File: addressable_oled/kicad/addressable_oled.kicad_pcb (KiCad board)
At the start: 2 copper layers, 1 part

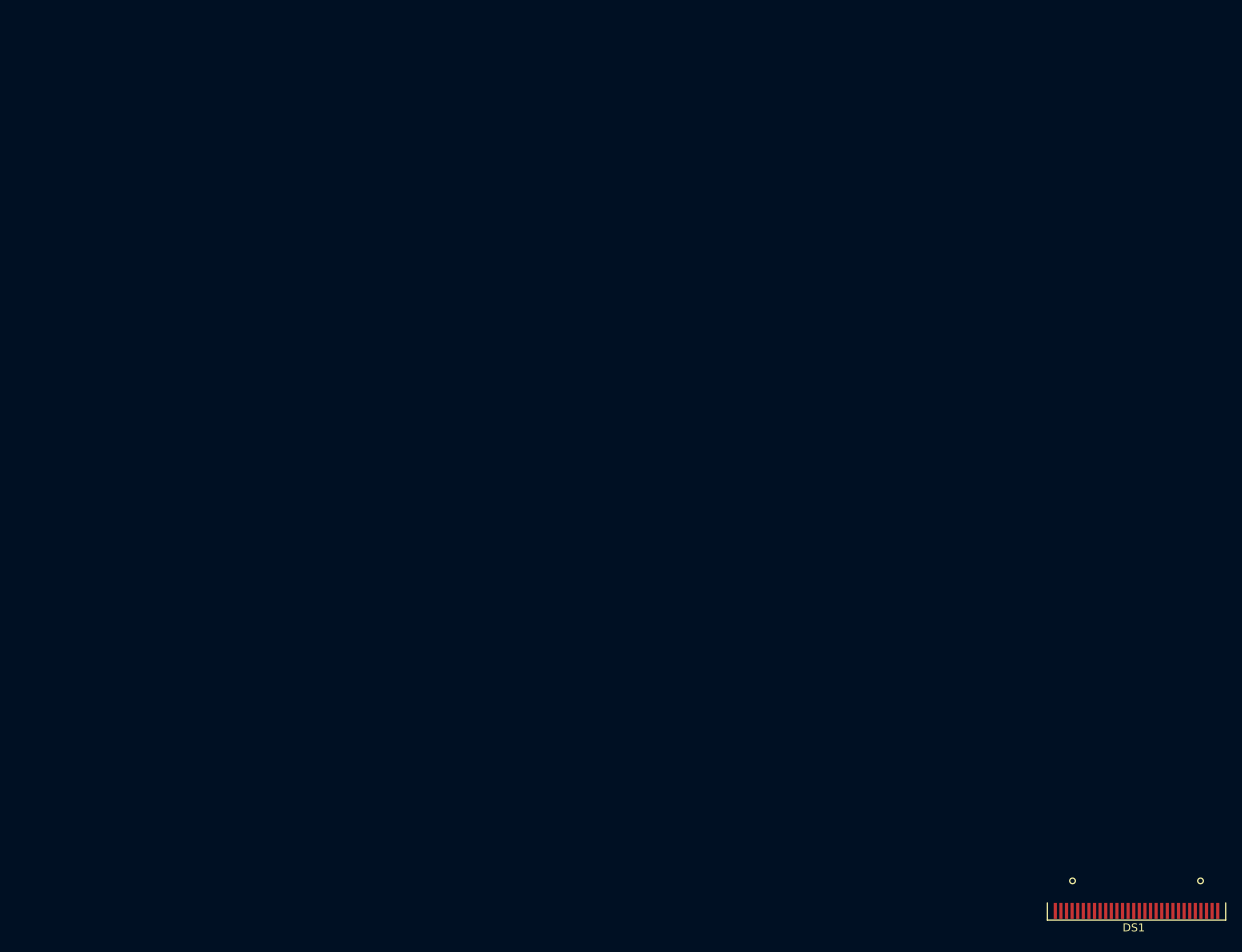
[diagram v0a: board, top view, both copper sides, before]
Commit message: Work in progress. Added symbols and footprints.
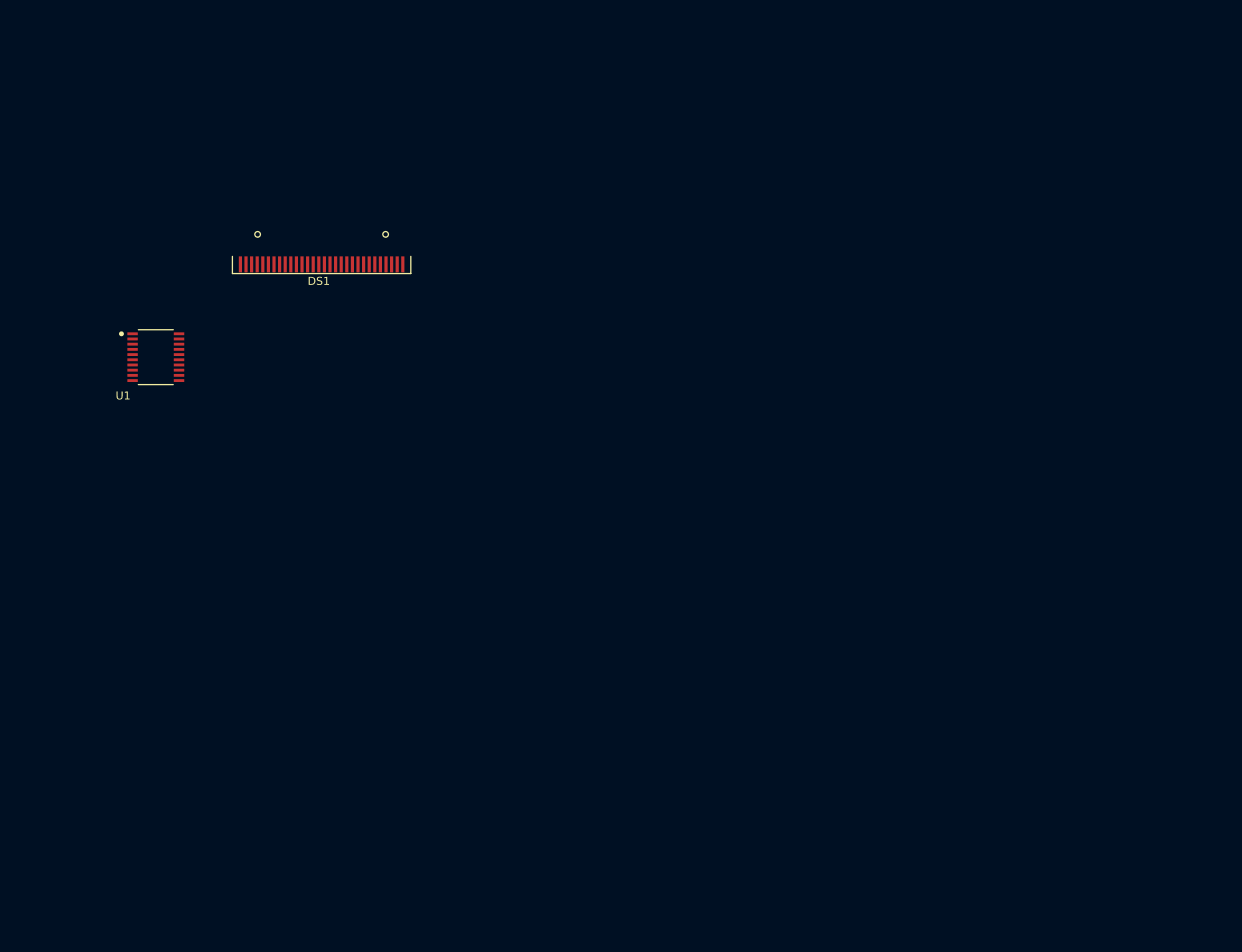
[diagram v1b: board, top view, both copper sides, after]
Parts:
- added U1: SLG46826G, addressable_oled:TSSOP20_MO-220_WECE_REN, F.Cu at (-1.32, 24.2)
- DS1: footprint Display:OLED-128O064D -> addressable_oled:OLED-128O064D
- moved DS1 130.0 mm to (19.4, 12.6)

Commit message: More progress with the schematic and layout.
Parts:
- added C1: 100n, Capacitor_SMD:C_0603_1608Metric, F.Cu at (-7.29, -11.4)
- added C2: 100n, Capacitor_SMD:C_0603_1608Metric, F.Cu at (-7.29, -8.90)
- added C3: 2u2, Capacitor_SMD:C_0603_1608Metric, F.Cu at (-7.29, -6.39)
- added C4: 1u, Capacitor_SMD:C_0603_1608Metric, F.Cu at (-7.29, -3.88)
- added C5: 1u, Capacitor_SMD:C_0603_1608Metric, F.Cu at (-3.28, -11.4)
- added C6: 100n, Capacitor_SMD:C_0603_1608Metric, F.Cu at (-3.28, -8.90)
- added C7: 100n, Capacitor_SMD:C_0603_1608Metric, F.Cu at (-3.28, -6.39)
- added C8: 100n, Capacitor_SMD:C_0603_1608Metric, F.Cu at (-3.28, -3.88)
- added C9: 2u2, Capacitor_SMD:C_0603_1608Metric, F.Cu at (0.73, -11.4)
- added J1: Conn_01x05_Pin, Connector_PinHeader_2.54mm:PinHeader_1x05_P2.54mm_Vertical, F.Cu at (15.1, -13.2)
- added J2: Conn_01x03_Socket, Connector_PinHeader_2.54mm:PinHeader_1x03_P2.54mm_Vertical, F.Cu at (42.4, 4.19)
- added JP1: Jumper_2_Open, Jumper:SolderJumper-2_P1.3mm_Open_Pad1.0x1.5mm, F.Cu at (35.8, -7.26)
- added JP2: Jumper_2_Open, Jumper:SolderJumper-2_P1.3mm_Open_Pad1.0x1.5mm, F.Cu at (33.3, -7.26)
- added JP4: Jumper_2_Open, Jumper:SolderJumper-2_P1.3mm_Open_Pad1.0x1.5mm, F.Cu at (30.7, -7.26)
- added R1: 5K, Resistor_SMD:R_0603_1608Metric, F.Cu at (0.73, -8.90)
- added R2: 5K, Resistor_SMD:R_0603_1608Metric, F.Cu at (0.73, -6.39)
- added R3: 910K, Resistor_SMD:R_0603_1608Metric, F.Cu at (0.73, -3.88)
- moved U1 37.8 mm to (21.9, -5.59)
- renumbered DS1 to U2
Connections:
- U1 pad 1: unconnected-(U1-IO14-Pad1) -> /CS
- U1 pad 10: unconnected-(U1-GND-Pad10) -> GND
- U1 pad 12: unconnected-(U1-SDA-Pad12) -> /I2C_DAT
- U1 pad 13: unconnected-(U1-SCL-Pad13) -> /I2C_CLK
- U1 pad 15: unconnected-(U1-IO4-Pad15) -> Net-(U1-IO4)
- U1 pad 16: unconnected-(U1-IO3-Pad16) -> Net-(U1-IO3)
- U1 pad 17: unconnected-(U1-IO2-Pad17) -> Net-(U1-IO2)
- U1 pad 2: unconnected-(U1-IO13-Pad2) -> /CLK
- U1 pad 20: unconnected-(U1-VDD-Pad20) -> VDD
- U1 pad 3: unconnected-(U1-IO12-Pad3) -> /MOSI
- U1 pad 4: unconnected-(U1-IO11-Pad4) -> /OLED_CS
- U1 pad 5: unconnected-(U1-IO10-Pad5) -> /OLED_CLK
- U1 pad 6: unconnected-(U1-IO9-Pad6) -> /OLED_MOSI
- U1 pad 7: unconnected-(U1-VDD2-Pad7) -> VDD
- U1 pad 8: unconnected-(U1-IO8-Pad8) -> /OLED_RST
- U1 pad 9: unconnected-(U1-IO7-Pad9) -> /OLED_DC
- U2 pad 1: Net-(DS1-GND-Pad1) -> GND
- U2 pad 10: unconnected-(DS1-BS0-Pad10) -> GND
- U2 pad 11: unconnected-(DS1-BS1-Pad11) -> GND
- U2 pad 12: unconnected-(DS1-BS2-Pad12) -> GND
- U2 pad 13: unconnected-(DS1-~{CS}-Pad13) -> /OLED_CS
- U2 pad 14: unconnected-(DS1-~{RES}-Pad14) -> /OLED_RST
- U2 pad 15: unconnected-(DS1-D/~{C}-Pad15) -> /OLED_DC
- U2 pad 16: unconnected-(DS1-R/~{W}-Pad16) -> GND
- U2 pad 17: unconnected-(DS1-E/~{RD}-Pad17) -> GND
- U2 pad 18: unconnected-(DS1-D0-Pad18) -> /OLED_CLK
- U2 pad 19: unconnected-(DS1-D1-Pad19) -> /OLED_MOSI
- U2 pad 2: unconnected-(DS1-C2N-Pad2) -> Net-(U2-C2N)
- U2 pad 21: unconnected-(DS1-D3-Pad21) -> GND
- U2 pad 22: unconnected-(DS1-D4-Pad22) -> GND
- U2 pad 23: unconnected-(DS1-D5-Pad23) -> GND
- U2 pad 24: unconnected-(DS1-D6-Pad24) -> GND
- U2 pad 25: unconnected-(DS1-D7-Pad25) -> GND
- U2 pad 26: unconnected-(DS1-IREF-Pad26) -> Net-(U2-IREF)
- U2 pad 27: unconnected-(DS1-VCOMH-Pad27) -> Net-(U2-VCOMH)
- U2 pad 28: unconnected-(DS1-VCC-Pad28) -> Net-(U2-VCC)
- U2 pad 29: unconnected-(DS1-VLSS-Pad29) -> GND
- U2 pad 3: unconnected-(DS1-C2P-Pad3) -> Net-(U2-C2P)
- U2 pad 30: Net-(DS1-GND-Pad1) -> GND
- U2 pad 4: unconnected-(DS1-C1P-Pad4) -> Net-(U2-C1P)
- U2 pad 5: unconnected-(DS1-C1N-Pad5) -> Net-(U2-C1N)
- U2 pad 6: unconnected-(DS1-VBAT-Pad6) -> VDD
- U2 pad 8: unconnected-(DS1-VSS-Pad8) -> GND
- U2 pad 9: unconnected-(DS1-VDD-Pad9) -> VDD

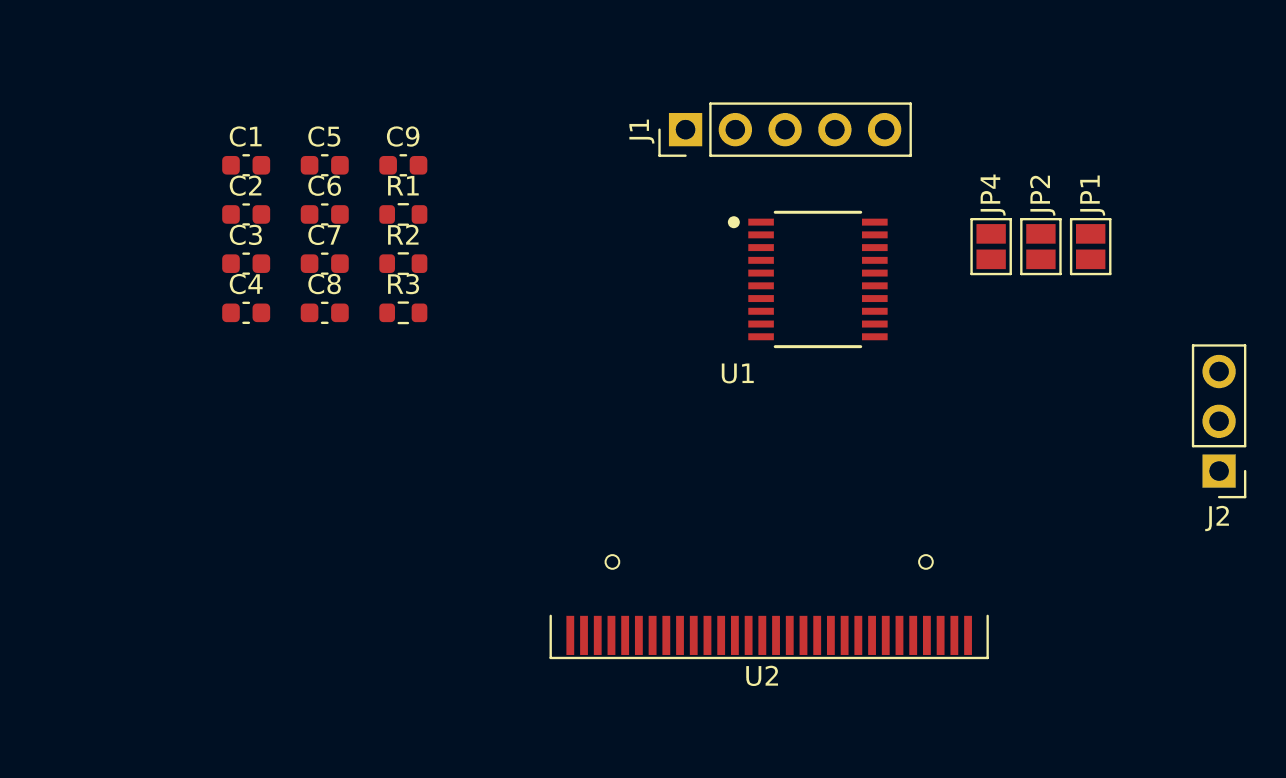
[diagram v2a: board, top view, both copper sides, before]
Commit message: Schematic and layout in progress. Added GreenPAK pullup pins.
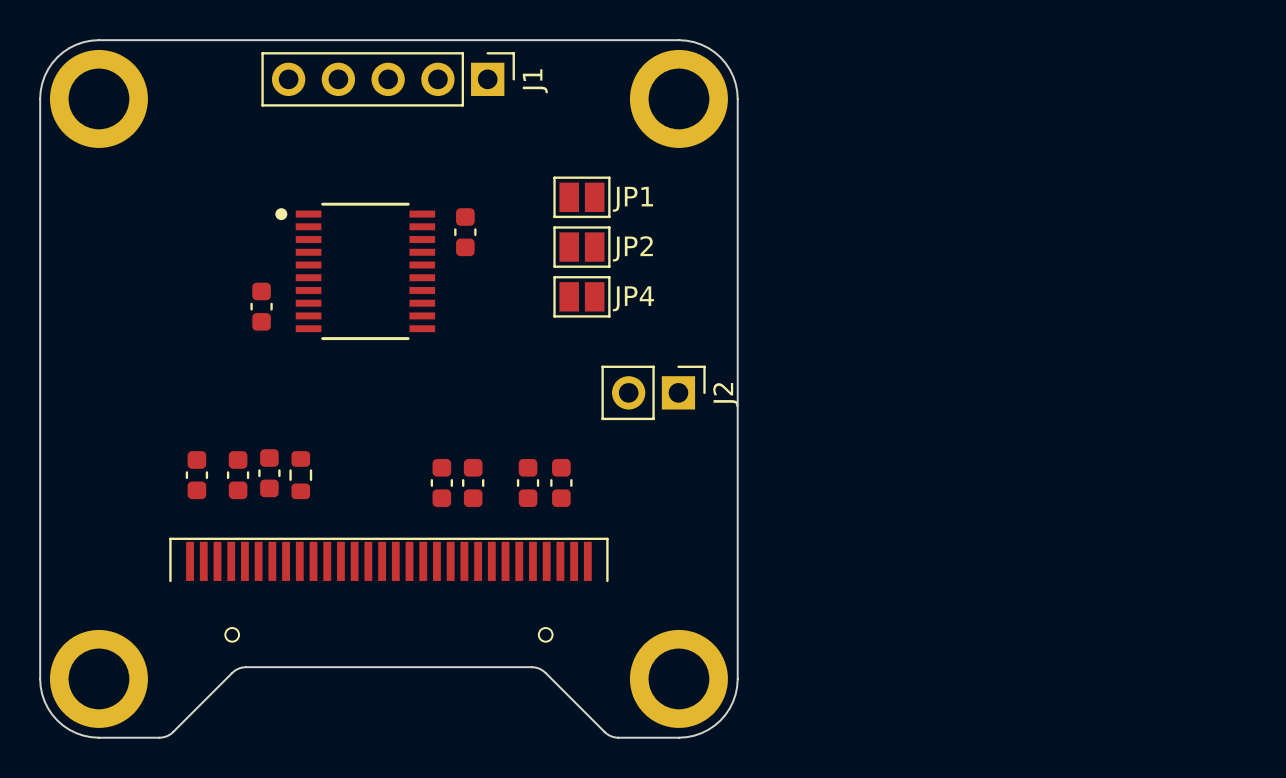
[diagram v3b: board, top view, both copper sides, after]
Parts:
- removed R1, R2: 5K, Resistor_SMD:R_0603_1608Metric
- added H1: MountingHole, addressable_oled:MountingHole, F.Cu at (-14.8, -14.8)
- added H2: MountingHole, addressable_oled:MountingHole, F.Cu at (14.8, -14.8)
- added H3: MountingHole, addressable_oled:MountingHole, F.Cu at (14.8, 14.8)
- added H4: MountingHole, addressable_oled:MountingHole, F.Cu at (-14.8, 14.8)
- J2: footprint Connector_PinHeader_2.54mm:PinHeader_1x03_P2.54mm_Vertical -> Connector_PinHeader_2.54mm:PinHeader_1x02_P2.54mm_Vertical
- moved J2 27.9 mm to (14.8, 0.20), turned to -90 degrees
- moved JP1 26.1 mm to (9.85, -9.78), turned to 0 degrees
- moved JP2 23.4 mm to (9.85, -7.24), turned to 0 degrees
- moved U1 23.1 mm to (-1.20, -6.00)
- moved JP4 21.0 mm to (9.85, -4.70), turned to 0 degrees
- moved U2 19.8 mm to (0.00, 8.80), turned to 180 degrees
- moved C5 19.3 mm to (7.10, 4.80), turned to 90 degrees
- moved C4 18.3 mm to (8.80, 4.80), turned to 90 degrees
- moved C9 17.9 mm to (-7.70, 4.40), turned to 90 degrees
- moved C6 15.7 mm to (4.30, 4.80), turned to 90 degrees
- moved C7 12.7 mm to (2.70, 4.80), turned to 90 degrees
- moved C2 11.2 mm to (3.90, -8.00), turned to -90 degrees
- moved C3 10.8 mm to (-6.10, 4.30), turned to -90 degrees
- moved C8 10.5 mm to (-9.80, 4.40), turned to 90 degrees
- moved J1 10.4 mm to (5.04, -15.8), turned to -90 degrees
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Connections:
- J2 pad 1: GND -> /I2C_DAT
- J2 pad 2: /I2C_DAT -> /I2C_CLK
- U1 pad 14: unconnected-(U1-IO5-Pad14) -> /I2C_CLK
- U1 pad 18: unconnected-(U1-IO1-Pad18) -> /I2C_DAT
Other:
- board outline added: 35.6 x 35.6 mm

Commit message: More progress with the layout.
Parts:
- C1, C2, C3, C4, C5, C6, C7, C8, C9: footprint Capacitor_SMD:C_0603_1608Metric -> addressable_oled:C_0603_1608Metric
- J1: footprint Connector_PinHeader_2.54mm:PinHeader_1x05_P2.54mm_Vertical -> addressable_oled:PinHeader_1x05_P2.54mm_Vertical
- J2: footprint Connector_PinHeader_2.54mm:PinHeader_1x02_P2.54mm_Vertical -> addressable_oled:PinHeader_1x04_P2.54mm_Vertical
- JP1, JP2, JP4: footprint Jumper:SolderJumper-2_P1.3mm_Open_Pad1.0x1.5mm -> addressable_oled:SolderJumper-2_P1.3mm_Open_Pad1.0x1.5mm
- R3: footprint Resistor_SMD:R_0603_1608Metric -> addressable_oled:R_0603_1608Metric
- moved J2 8.55 mm to (15.6, 8.71), turned to 180 degrees
- moved C9 2.10 mm to (-9.80, 4.40)
- moved JP1 2.02 mm to (8.67, -8.14)
- moved C8 1.80 mm to (-8.00, 4.40)
- moved JP2 1.65 mm to (8.67, -6.08)
- moved JP4 1.35 mm to (8.67, -4.04)
- moved C6 1.26 mm to (5.50, 4.40), turned to -90 degrees
- moved C7 1.08 mm to (3.70, 4.40), turned to -90 degrees
- moved C2 0.77 mm to (4.56, -8.40), turned to 90 degrees
- moved U1 0.66 mm to (-0.55, -6.09)
- moved C1 0.57 mm to (-5.93, -4.15)
- moved C4 0.50 mm to (9.10, 4.40), turned to -90 degrees
- moved C5 0.45 mm to (7.30, 4.40)
- moved C3 0.14 mm to (-6.20, 4.40)
- moved R3 0.10 mm to (-4.40, 4.40)
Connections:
- J2 pad 1: /I2C_DAT -> GND
- J2 pad 2: /I2C_CLK -> VDD
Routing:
- net VDD: track 0.00 -> 75.0 mm
- net GND: track 0.00 -> 39.7 mm, vias 0 -> 14
- net /I2C_DAT: track 0.00 -> 22.9 mm, vias 0 -> 2
- net /OLED_CLK: track 0.00 -> 19.3 mm, vias 0 -> 2
- net /OLED_CS: track 0.00 -> 18.6 mm
- net /OLED_MOSI: track 0.00 -> 18.5 mm, vias 0 -> 2
- net /I2C_CLK: track 0.00 -> 17.8 mm, vias 0 -> 2
- net /OLED_RST: track 0.00 -> 15.6 mm
- net /OLED_DC: track 0.00 -> 14.7 mm
- net /MOSI: track 0.00 -> 11.2 mm, vias 0 -> 2
- net /CLK: track 0.00 -> 9.23 mm, vias 0 -> 2
- net /CS: track 0.00 -> 8.61 mm, vias 0 -> 2
- net Net-(U1-IO4): track 0.00 -> 6.38 mm
- net Net-(U1-IO2): track 0.00 -> 6.31 mm
- net Net-(U2-C1N): track 0.00 -> 5.98 mm
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- added copper zone on B.Cu, net GND
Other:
- board text added: "A0"
- board text added: "A1"
- board text added: "A2"
- board text added: "ADDRESS"
- board text added: "CLK"
- board text added: "CS"
- board text added: "GND"
- board text added: "MOS"
- board text added: "PROG"
- board text added: "SCL"
- board text added: "SDA"
- board text added: "VCC"
- board text added: "locked"

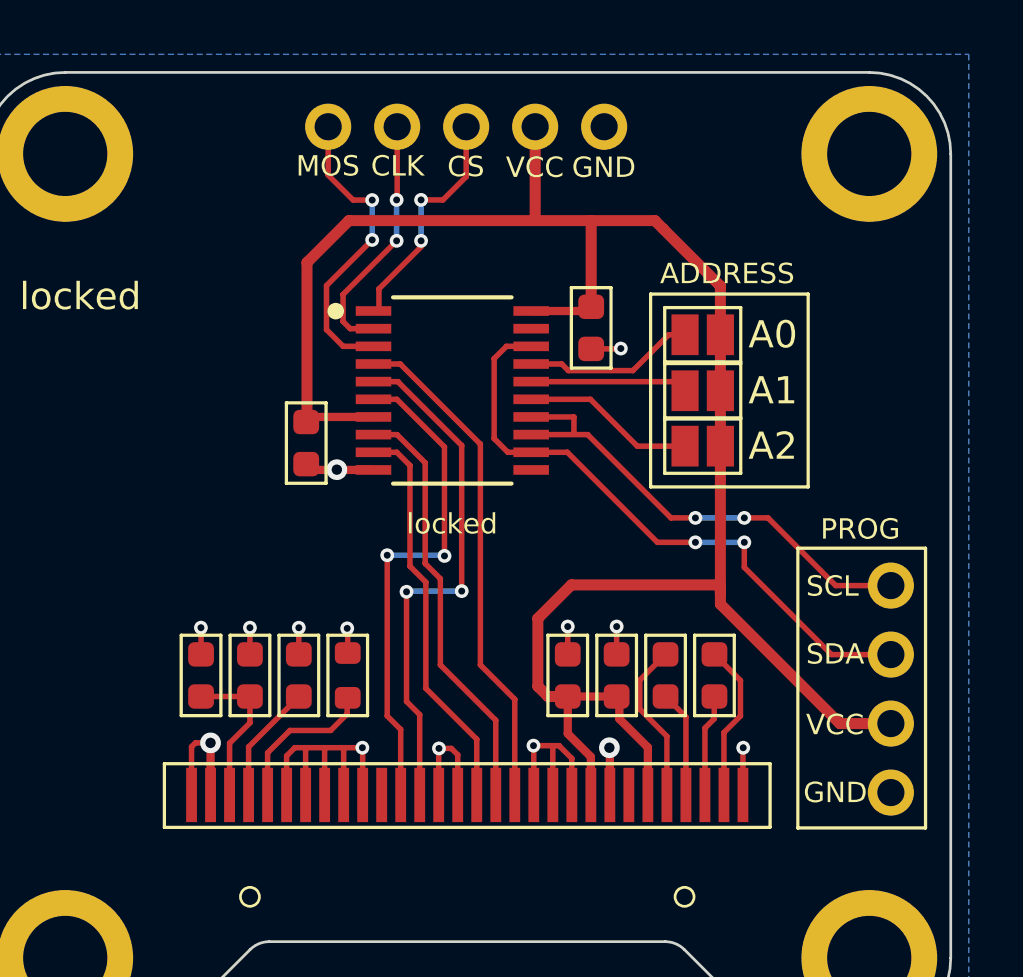
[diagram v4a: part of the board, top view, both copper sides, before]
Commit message: Switched from kicad 7.0.1-0 to 7.0.10.
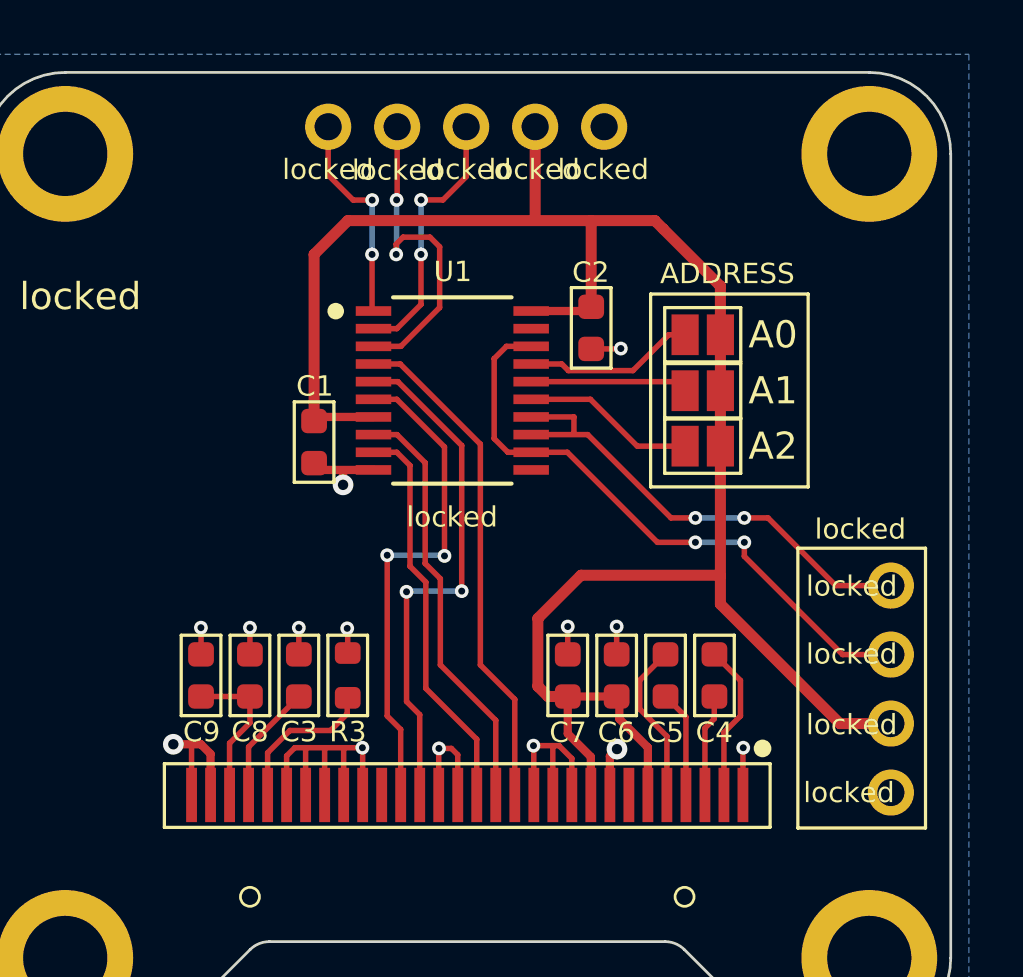
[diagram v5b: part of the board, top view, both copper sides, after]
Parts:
- moved C1 0.29 mm to (-5.64, -4.19)
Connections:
- J1 pad 3: /CS -> /CLK
- J1 pad 4: /CLK -> /MOSI
- J1 pad 5: /MOSI -> /CS
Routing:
- net GND: track 39.7 -> 40.7 mm
- net /MOSI: track 11.2 -> 12.2 mm
- net /CS: track 8.61 -> 7.89 mm
- net VDD: track 75.0 -> 74.3 mm
- net /CLK: track 9.23 -> 9.82 mm
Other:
- board text removed: "CLK"
- board text removed: "CS"
- board text removed: "GND"
- board text removed: "MOS"
- board text removed: "PROG"
- board text removed: "SCL"
- board text removed: "SDA"
- board text removed: "VCC"
